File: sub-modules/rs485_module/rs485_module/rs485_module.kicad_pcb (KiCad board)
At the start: 2 copper layers, 50 x 19.4 mm, 14 parts, among them J1 Conn_02x06_Odd_Even, J2 TX_EN_Sel, J3 TX Pol, J4 RX Pol, J5 TERM_EN, J6 RS422/485, J9 MKDS 1/ 5-3,5, U1 74LVC1GU04DRL, U2 ADM3491ExR

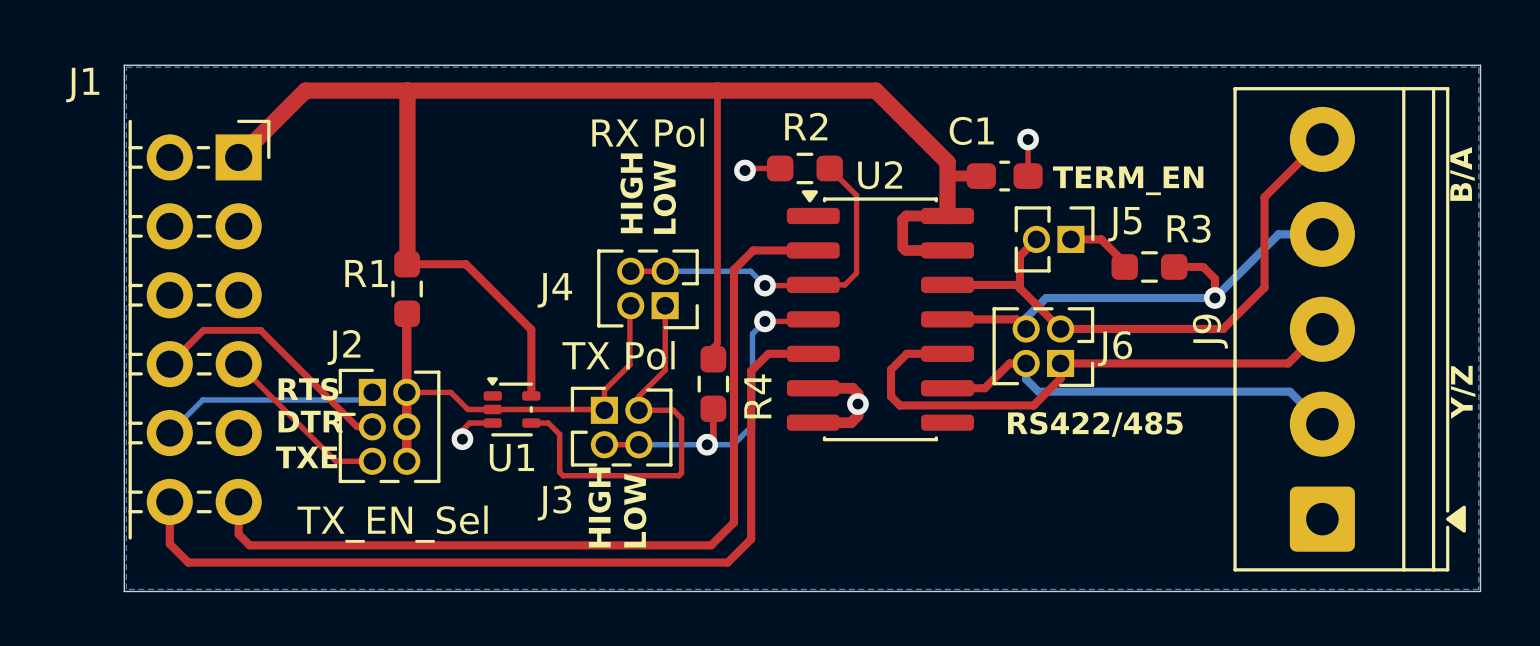
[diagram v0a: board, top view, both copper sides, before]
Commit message: Update schematics after moving to KiCad 10
Added some footprints to a local lib, as the silkscreen caused issues.

Signed-off-by: Marc Kelly <mpkelly@achenar.co.uk>
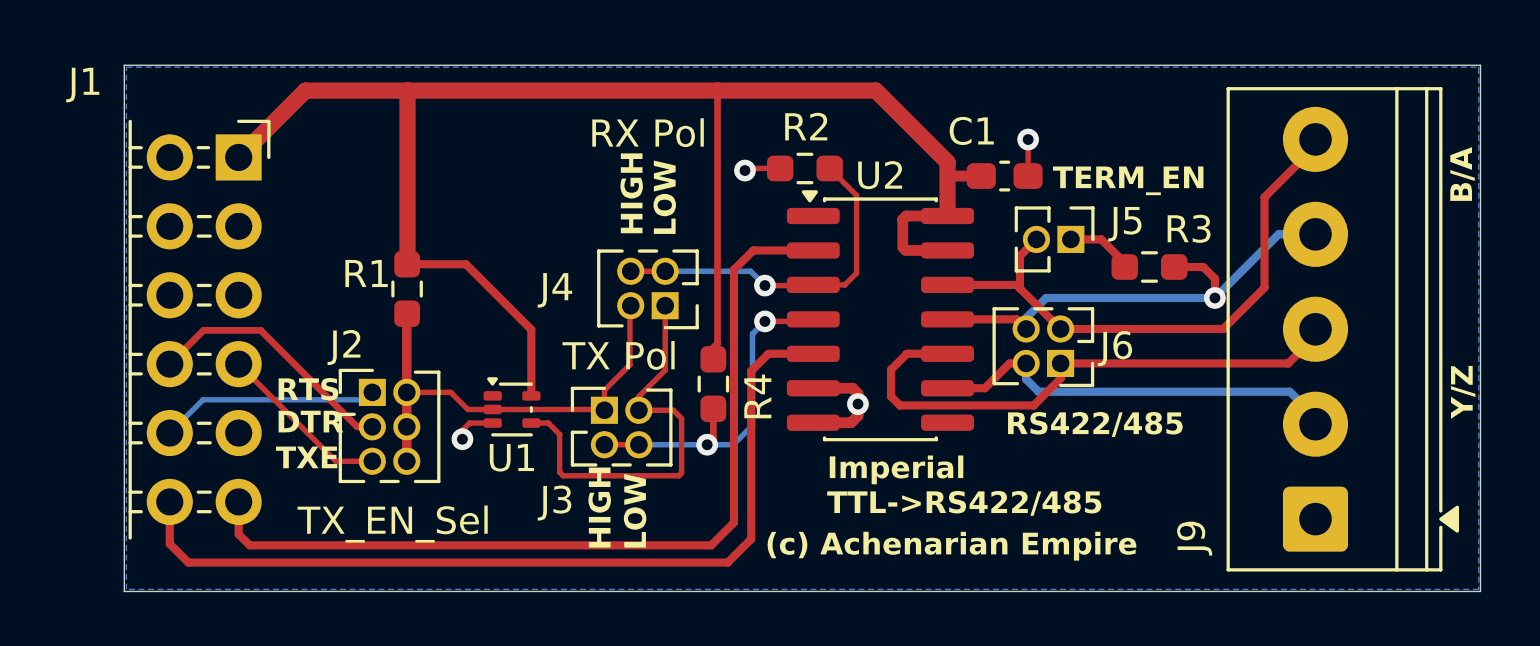
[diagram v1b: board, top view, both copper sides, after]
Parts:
- moved J9 0.25 mm to (94.7, 73.5)
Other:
- board text added: "(c) Achenarian Empire"
- board text added: "Imperial TTL->RS422/485"
